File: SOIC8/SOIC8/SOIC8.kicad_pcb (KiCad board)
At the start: 2 copper layers, 10.2 x 10.2 mm, 5 parts, among them J1 Conn_01x04, J2 Conn_01x04, J3 SOIC8, J4 VSSOP8

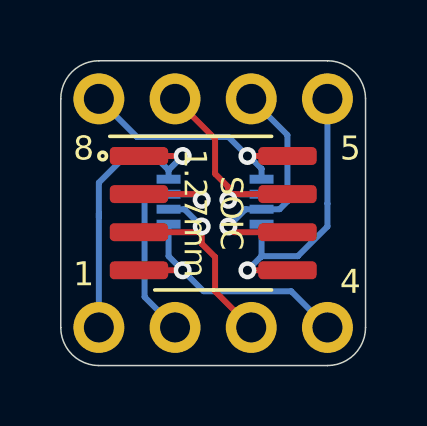
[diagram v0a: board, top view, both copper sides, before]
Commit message: Breakout Boards Revision 2
Renders updated, silkscreen text improved, blurry silkscreen items removed/resized.
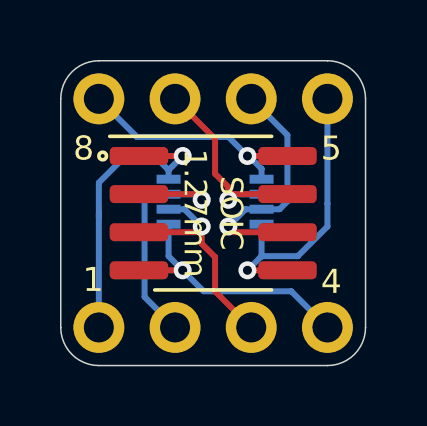
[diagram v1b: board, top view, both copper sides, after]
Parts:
- removed G***: LOGO, logo:SirBoard56x18
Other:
- board text added: "SirBoard"
